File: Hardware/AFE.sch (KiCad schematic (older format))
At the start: 46 parts, among them U801 4069.HEF4069UBTT,118, U802 MCP47CXBX2

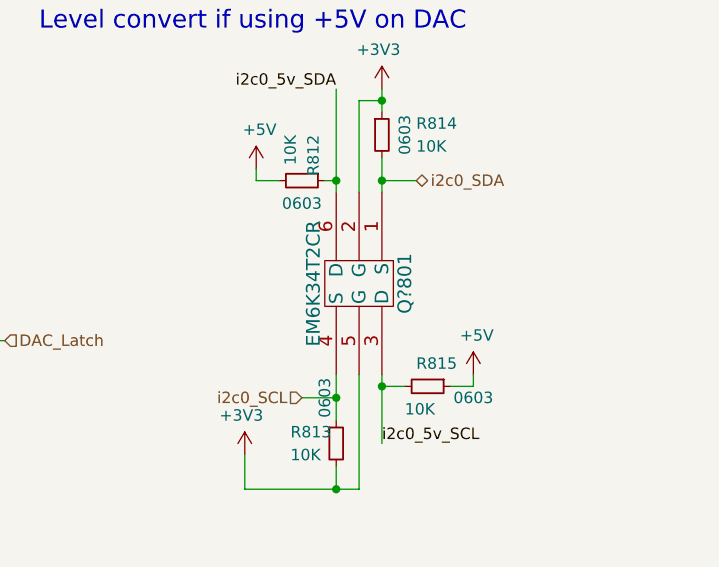
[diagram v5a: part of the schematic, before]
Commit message: Doing up some layout. Going to change SAO header to match.
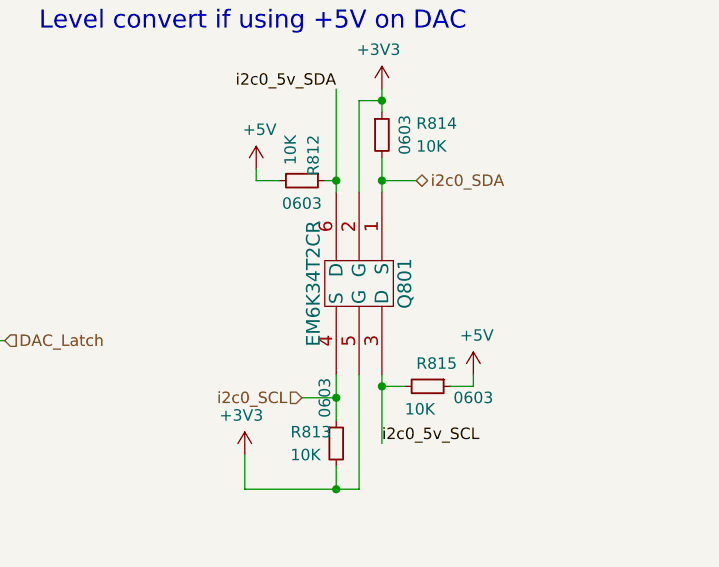
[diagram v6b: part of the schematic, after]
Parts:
- renumbered Q?801 to Q801
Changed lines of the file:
@@
 $Descr A4 11693 8268
 encoding utf-8
-Sheet 8 7
+Sheet 7 9
 Title ""
 Date ""
@@
 	1050 6900 1050 7000
 $Comp
-L OHMC2022:EM6K34T2CR Q?801
+L OHMC2022:EM6K34T2CR Q801
 U 1 1 613FBC97
 P 10200 4350
-F 0 "Q?801" H 10200 4550 60  0000 C CNN
+F 0 "Q801" H 10200 4550 60  0000 C CNN
 F 1 "EM6K34T2CR" H 10200 4150 60  0000 C CNN
 F 2 "OHMC2022:DualNFet.SOT563.EM6K34T2CR" H 11200 4590 60  0001 C CNN

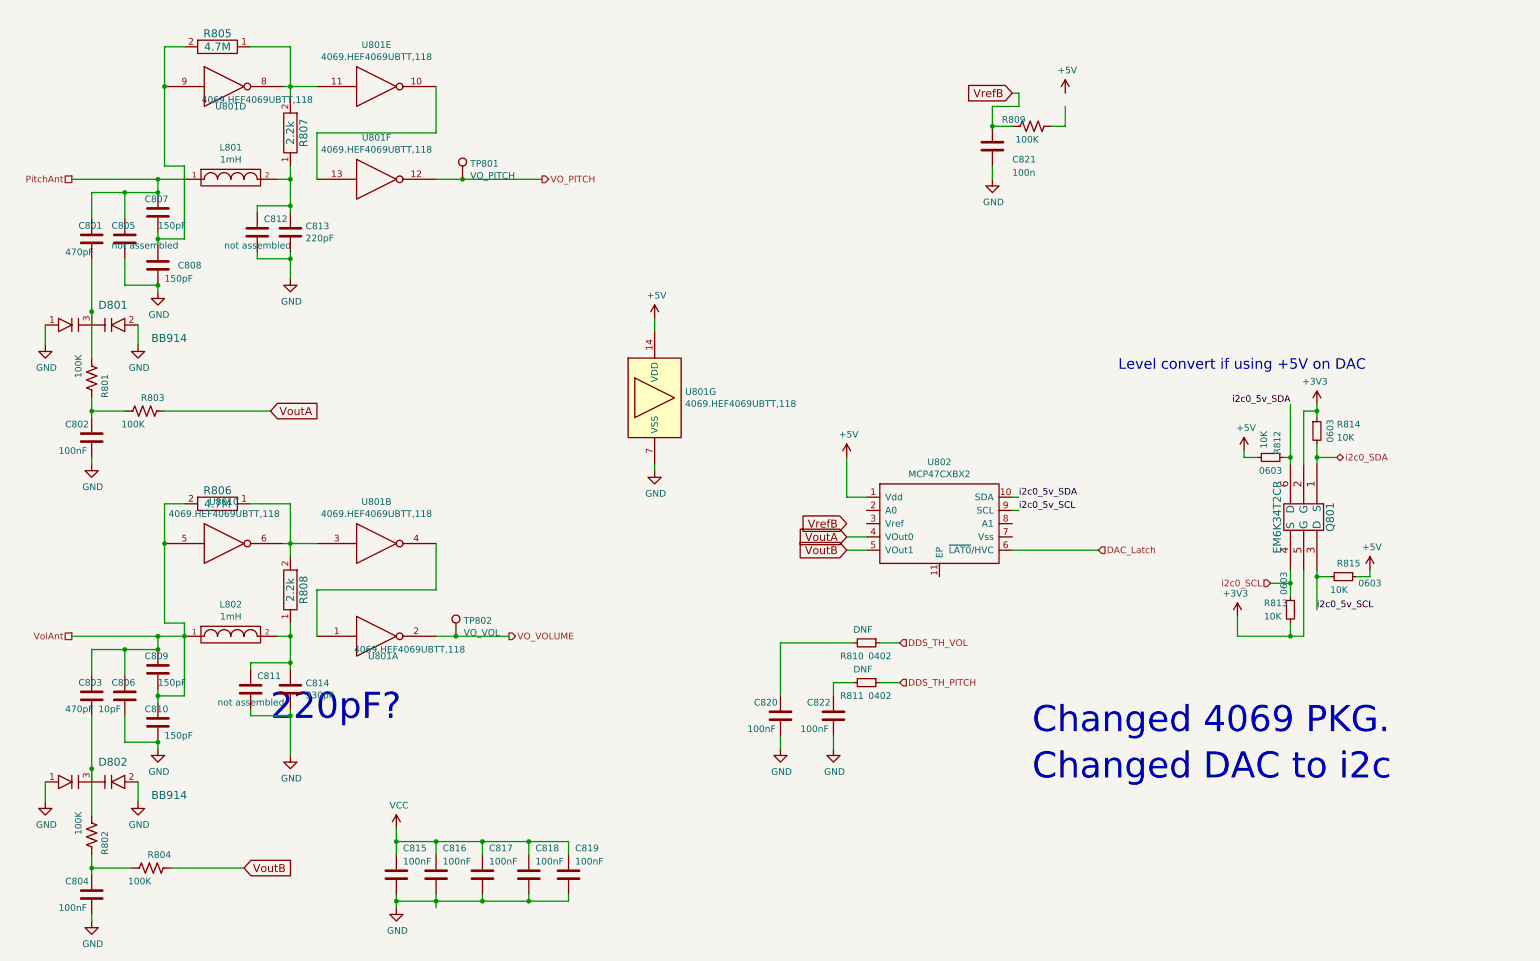
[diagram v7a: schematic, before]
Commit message: Think this is close to fixing the power circuitry.
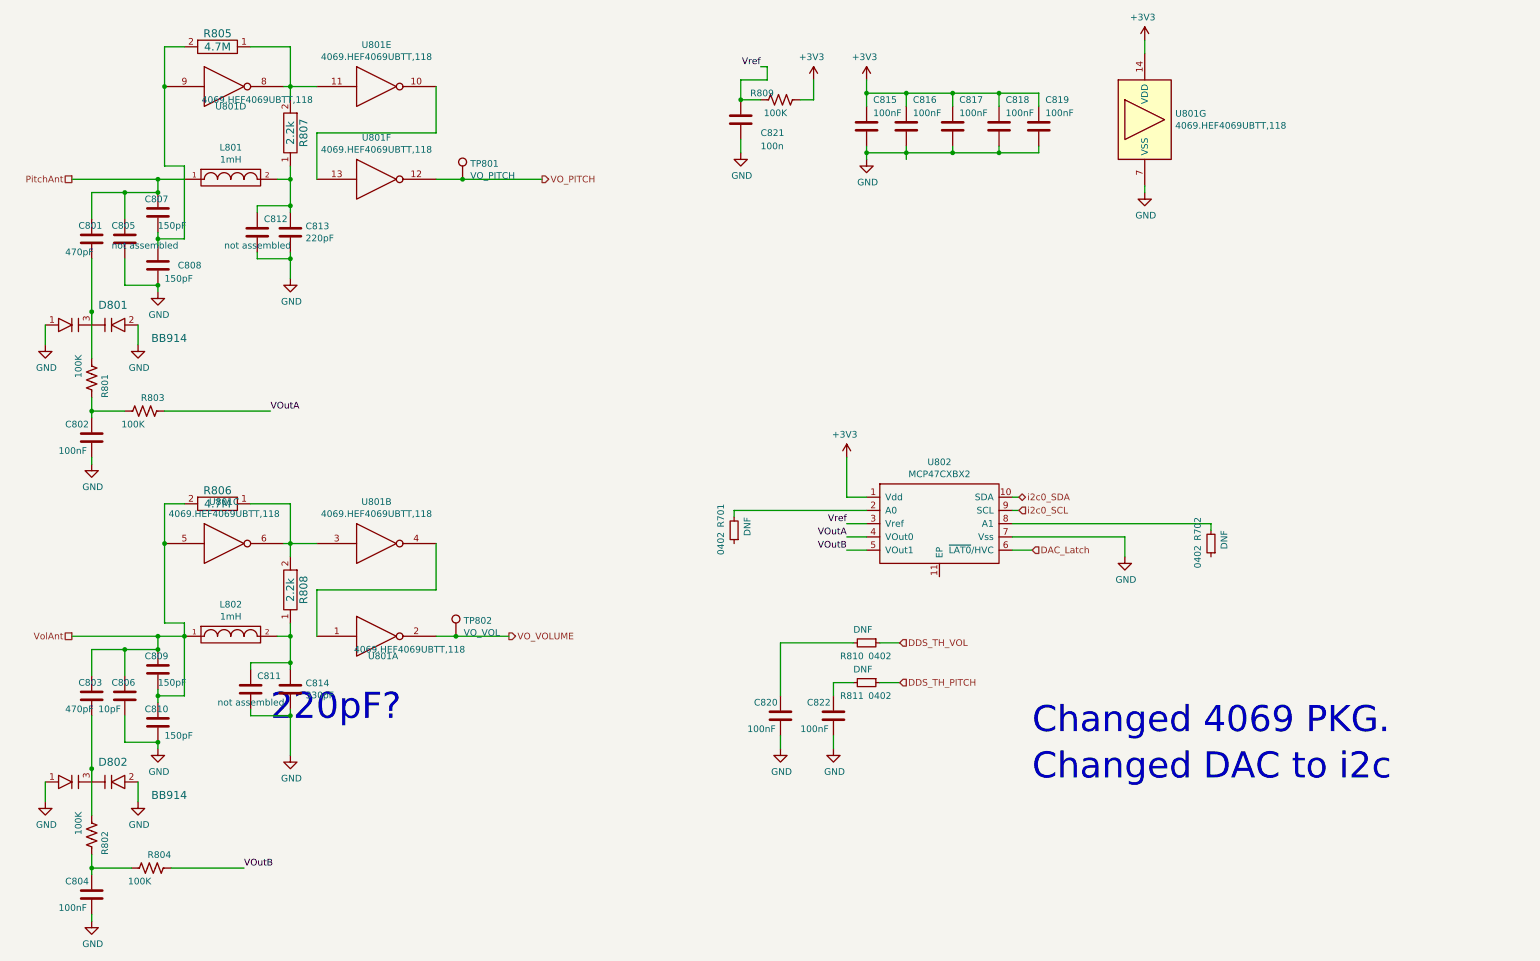
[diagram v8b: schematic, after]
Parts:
- removed Q801: EM6K34T2CR, OHMC2022:DualNFet.SOT563.EM6K34T2CR, symbol OHMC2022:EM6K34T2CR
- removed R812, R813, R814, R815: 10K, Resistor_SMD:R_0603_1608Metric, symbol Device:R_Small
- added R701, R702: DNF, Resistor_SMD:R_0402_1005Metric, symbol Device:R_Small
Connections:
- net VCC is gone; now on net +3V3: C815.1, C816.1, C817.1, C818.1, C819.1
- net VrefB is gone; now on net Vref: C821.1, R809.1
- net i2c0_5v_SCL is gone; now on net i2c0_SCL: U802.9 (SCL)
- net i2c0_5v_SDA is gone; now on net i2c0_SDA: U802.10 (SDA)
- net +3V3: now also R809.2, U801.14 (VDD), U802.1 (Vdd)
- net GND: now also U802.7 (Vss)
- net at U802.2 (A0): now also R701.2
- net Vref: now reaches U802.3 (Vref)
- net at U802.8 (A1): now also R702.2
- removed net +5V: U801.14 (VDD), U802.1 (Vdd)
- net VoutA renamed VOutA
- net VoutB renamed VOutB
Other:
- note removed: "Level convert if using +5V on DAC"
- moved on the sheet: C815, C816, C817, C818, C819, C821, R809, U801G
